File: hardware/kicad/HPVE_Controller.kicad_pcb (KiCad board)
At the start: 2 copper layers, 105 parts, among them U1 74HC595, U10 Raspberry_Pi_Pico, U101 TC4427ACOA, U102 TC4427ACOA, U103 TC4427ACOA, U104 TC4427ACOA, U105 TC4427ACOA, U106 TC4427ACOA, U107 TC4427ACOA, U108 TC4427ACOA, U109 TC4427ACOA, U110 TC4427ACOA, U111 TC4427ACOA, U112 TC4427ACOA, U113 TC4427ACOA, U114 TC4427ACOA, U115 TC4427ACOA, U116 TC4427ACOA, U117 TC4427ACOA, U118 TC4427ACOA, U119 TC4427ACOA, U120 TC4427ACOA, U121 TC4427ACOA, U122 TC4427ACOA, U123 TC4427ACOA, U124 TC4427ACOA, U125 TC4427ACOA, U126 TC4427ACOA, U127 TC4427ACOA, U128 TC4427ACOA, U129 TC4427ACOA, U130 TC4427ACOA, U131 TC4427ACOA, U132 TC4427ACOA, U2 74HC595, U3 74HC595, U4 74HC595, U5 74HC595, U6 74HC595, U7 74HC595, U8 74HC595

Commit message: Add 140x140mm Edge.Cuts border and 4x M3 chassis mounting holes
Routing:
- net (no net): vias 0 -> 4
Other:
- board outline added: 140 x 140 mm

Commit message: fix(hardware): optimize PCB outline to 108x88mm eliminating empty dead space and centering silkscreen
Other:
- board size 140 x 140 mm -> 108 x 88 mm
- board text added: "64-CHANNEL 40kHz PHASED ULTRASONIC EMITTER"
- board text added: "HPVE CONTROLLER MOTHERBOARD REV 1.0"
- board text added: "IRON CAVE INDUSTRIES | HACK CLUB FALLEN 2026"
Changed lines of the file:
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@@
 	)
 	(gr_line
-		(start 70 40)
-		(end 210 40)
+		(start 67 49)
+		(end 175 49)
 		(stroke
 			(width 0.15)
@@
 	)
 	(gr_line
-		(start 70 180)
-		(end 70 40)
+		(start 67 137)
+		(end 67 49)
 		(stroke
 			(width 0.15)
@@
 	)
 	(gr_line
-		(start 210 40)
-		(end 210 180)
+		(start 175 49)
+		(end 175 137)
 		(stroke
 			(width 0.15)
@@
 	)
 	(gr_line
-		(start 210 180)
-		(end 70 180)
+		(start 175 137)
+		(end 67 137)
 		(stroke
 			(width 0.15)
@@
 		(layer "Edge.Cuts")
 	)
+	(gr_text "IRON CAVE INDUSTRIES | HACK CLUB FALLEN 2026"
+		(at 121 53.8 0)
+		(layer "F.SilkS")
+		(effects
+			(font
+				(size 1 1)
+				(thickness 0.16)
+			)
+		)
+	)
+	(gr_text "64-CHANNEL 40kHz PHASED ULTRASONIC EMITTER"
+		(at 121 134.5 0)
+		(layer "F.SilkS")
+		(effects
+			(font
+				(size 1.1 1.1)
+				(thickness 0.18)
+			)
+		)
+	)
+	(gr_text "HPVE CONTROLLER MOTHERBOARD REV 1.0"
+		(at 121 51.5 0)
+		(layer "F.SilkS")
+		(effects
+			(font
+				(size 1.3 1.3)
+				(thickness 0.2)
+			)
+		)
+	)
 	(via
-		(at 75 45)
+		(at 171 53)
 		(size 6)
 		(drill 3.2)
@@
 	)
 	(via
-		(at 205 45)
+		(at 71 53)
 		(size 6)
 		(drill 3.2)
@@
 	)
 	(via
-		(at 205 175)
+		(at 171 133)
 		(size 6)
 		(drill 3.2)
@@
 	)
 	(via
-		(at 75 175)
+		(at 71 133)
 		(size 6)
 		(drill 3.2)

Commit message: feat(hardware): upgrade PCB to 45-degree mitered routing, dual-layer GND copper zones, and KiCad 2D editor render
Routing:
- net SIG_57: track 96.8 -> 68.5 mm
- net DRV_16: track 91.7 -> 67.1 mm
- net SIG_64: track 98.7 -> 74.8 mm
- net SIG_63: track 98.7 -> 74.8 mm
- net SIG_62: track 97.2 -> 73.3 mm
- net SIG_61: track 97.2 -> 73.3 mm
- net SIG_60: track 95.7 -> 71.8 mm
- net SIG_59: track 95.7 -> 71.8 mm
- net SIG_58: track 94.2 -> 70.3 mm
- net DRV_15: track 84.5 -> 61.5 mm
- net GND: track 531.4 -> 510.5 mm
- net DRV_14: track 75.9 -> 55.2 mm
- net SIG_41: track 83.7 -> 63.0 mm
- net DRV_32: track 99.0 -> 78.7 mm
- net DRV_11: track 110.6 -> 91.1 mm
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- added copper zone on B.Cu, net GND
- added copper zone on F.Cu, net GND

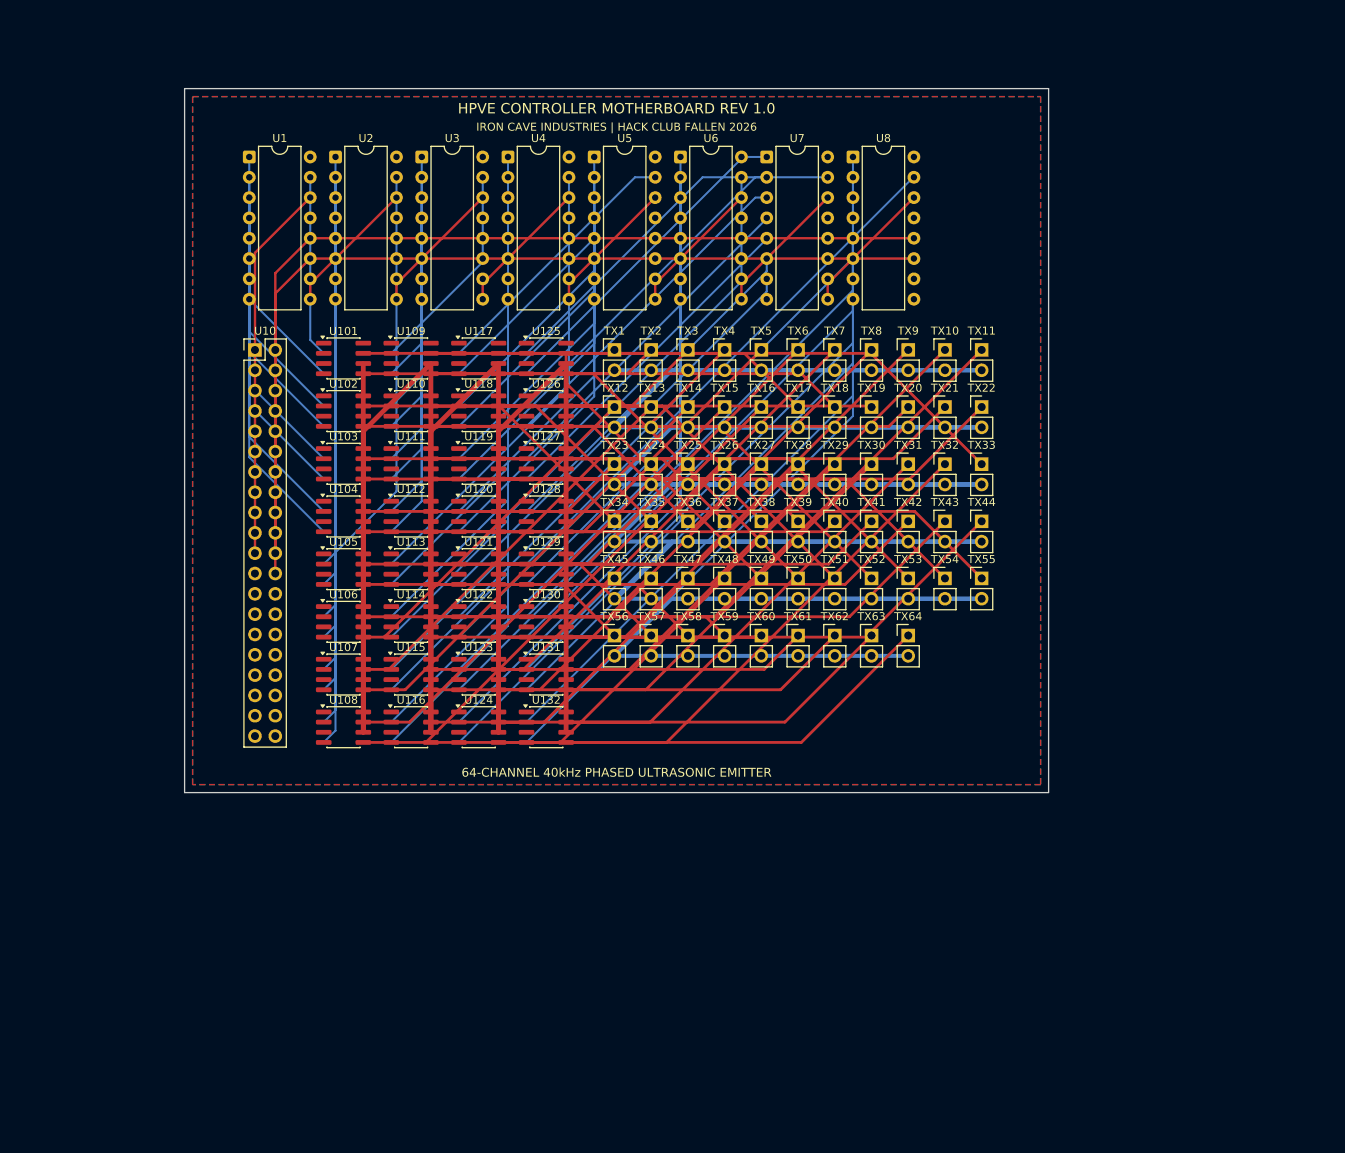
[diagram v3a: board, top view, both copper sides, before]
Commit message: fix(hardware): replace male headers with official Pico module and flush transducer pads; polish 3D and 2D renders
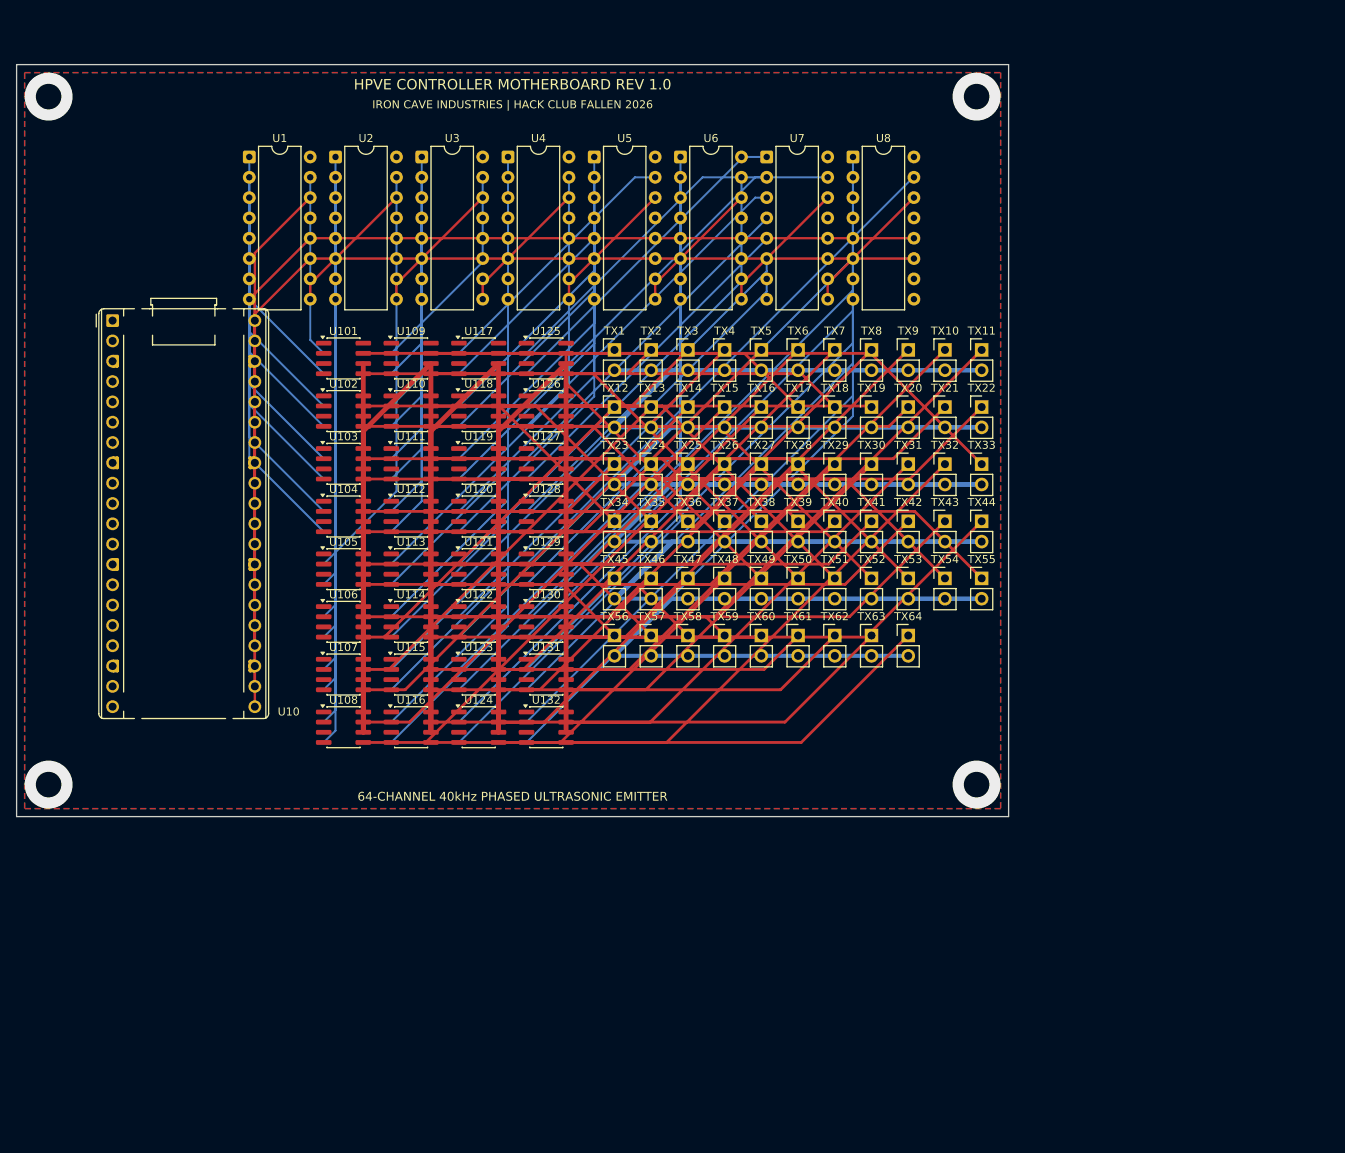
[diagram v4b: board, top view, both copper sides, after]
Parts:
- U10: value Raspberry_Pi_Pico -> RP2040_Pico; footprint Connector_PinHeader_2.54mm:PinHeader_2x20_P2.54mm_Vertical -> RaspberryPi_Pico_Common_THT
- moved U10 18.2 mm to (58.0, 78.0)
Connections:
- U10 pad 38: /RP2040_Core_UI/GND -> GND
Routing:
- net SPI_MOSI: track 47.3 -> 66.5 mm
- net SPI_SCK: track 114.1 -> 131.8 mm
- net SPI_LATCH: track 119.2 -> 129.3 mm
- net (no net): vias 0 -> 4
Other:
- board size 108 x 88 mm -> 124 x 94 mm
